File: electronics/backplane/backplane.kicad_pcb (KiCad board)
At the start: 2 copper layers, 46 x 100 mm, 63 parts, among them J1 USB_C_SOCKET_RA_PTH_SIMPLE, P1 PAD_SOLDER_2mm, P10 CONN_01X03, P11 PAD_SOLDER_2mm, P12 PAD_SOLDER_2mm, P13 PAD_SOLDER_2mm, P14 PAD_SOLDER_2mm, P15 PAD_SOLDER_2mm, P16 PAD_SOLDER_2mm, P2 JST_SH_4_RA, P3 JST_SH_4_RA, P4 JST_SH_4_RA, P5 PAD_SOLDER_2mm, P6 PAD_SOLDER_2mm, P7 PAD_SOLDER_2mm, P8 PAD_SOLDER_2mm, P9 PAD_SOLDER_2mm, Q1 2N7002P, SW1 B3U-1000P_SPST-NO_SMD, SW2 B3U-1000P_SPST-NO_SMD, U1 USBLC6, U9 AP2112K-3.3, X1 MICROMOD_PROCESSOR_SOCKET, X2 SWD_SMT_SOCKET, X3 MICROMOD_FUNCTION_BOARD_SOCKET

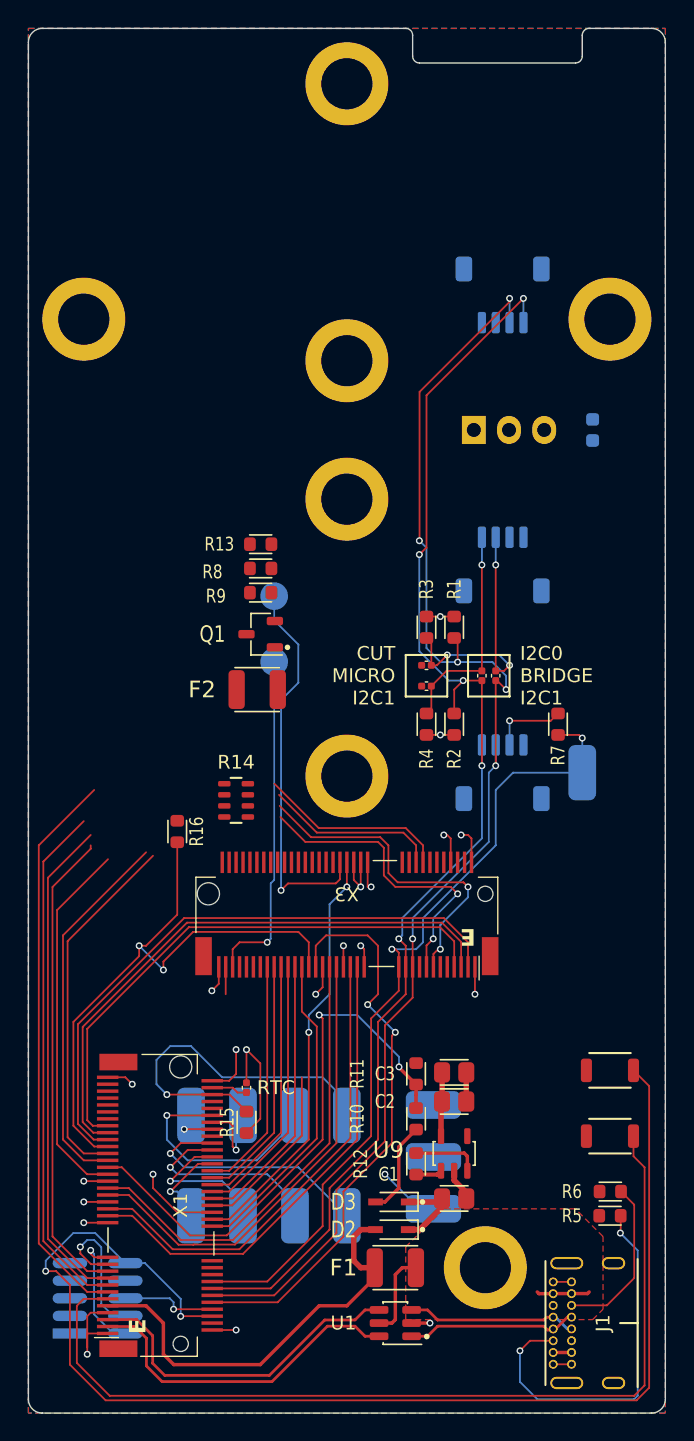
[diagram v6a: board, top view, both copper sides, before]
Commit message: Backplane routing complete General schematic cleanup, board cosmetics etc
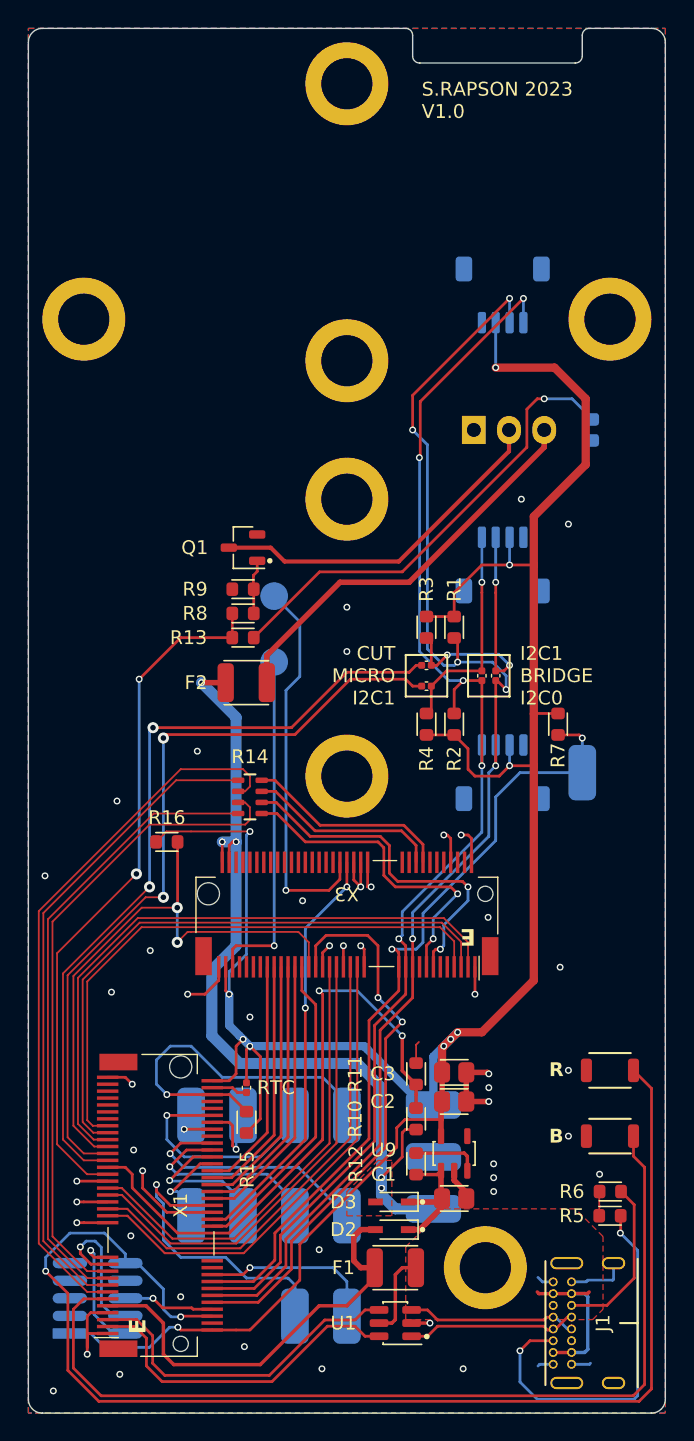
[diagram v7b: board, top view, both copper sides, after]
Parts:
- added P17: PAD_SOLDER_2mm, Applidyne_Connector:PAD_SOLDER_2mm, B.Cu at (123.0, 143.0)
- added P18: PAD_SOLDER_2mm, Applidyne_Connector:PAD_SOLDER_2mm, B.Cu at (119.2, 143.0)
- moved R13 6.87 mm to (115.5, 94.0)
- moved Q1 6.38 mm to (115.5, 87.5)
- moved R8 3.49 mm to (115.5, 92.2), turned to 0 degrees
- moved R9 1.30 mm to (115.5, 90.5), turned to 180 degrees
- moved R16 1.06 mm to (110.0, 108.8), turned to 0 degrees
- moved R14 1.03 mm to (116.0, 105.5)
- moved F2 0.93 mm to (115.7, 97.2)
- turned D1 to 90 degrees
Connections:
- X1 pad 65: /Processor/G9 -> unconnected-(X1-G9/ADC_D-/CAM_HSYNC-Pad65)
- X1 pad 67: /Processor/G8 -> unconnected-(X1-G8-Pad67)
- X1 pad 69: /Processor/G7 -> unconnected-(X1-G7/BUS7-Pad69)
- X1 pad 71: /Processor/G6 -> unconnected-(X1-G6/BUS6-Pad71)
- X1 pad 73: /Processor/G5 -> unconnected-(X1-G5/BUS5-Pad73)
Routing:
- net +3.3V: track 31.0 -> 192.8 mm, vias 6 -> 11
- net +POWER: track 11.4 -> 64.0 mm, vias 1 -> 5
- net Net-(D1-PadA): track 0.00 -> 33.8 mm, vias 0 -> 1
- net Net-(X1-I2C_SDA1): track 27.1 -> 57.6 mm, vias 0 -> 2
- net Net-(X1-I2C_SCL1): track 26.3 -> 56.4 mm, vias 0 -> 2
- net Net-(P10-P3): track 0.00 -> 29.5 mm
- net Net-(P10-P2): track 0.00 -> 25.5 mm
- net /Expansion IO/PWM_OUTPUT: track 26.7 -> 50.3 mm, vias 0 -> 2
- net GND: track 48.7 -> 64.5 mm, vias 16 -> 47
- net /Expansion IO/DIGITAL_OUT: track 0.00 -> 12.8 mm, vias 0 -> 1
- net /Function Board/RX: track 34.4 -> 47.0 mm
- net /Function Board/RTS: track 40.8 -> 51.9 mm
- net /Function Board/CTS: track 37.5 -> 47.7 mm
- net /Function Board/TX: track 35.9 -> 45.5 mm
- net /Expansion IO/ANALOG_IN: track 12.8 -> 22.2 mm, vias 0 -> 1
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- added copper zone on F.Cu, net +POWER
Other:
- board text added: "2 Layer 1.6mm board thickness 1oz copper 100 x 46 mm White Soldermask Black Silkscreen"
- board text added: "A1"
- board text added: "B"
- board text added: "D1"
- board text added: "I2C1 BRIDGE I2C0"
- board text added: "PCB MANUFACTURE NOTES"
- board text added: "R"
- board text added: "S.RAPSON 2023 V1.0"
- board text added: "SPI1"
- board text removed: "I2C0 BRIDGE I2C1"
